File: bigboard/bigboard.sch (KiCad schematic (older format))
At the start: 38 parts, among them J1 motorA, J2 motorB, J3 USB_B_Mini, J4 device2, J5 device1, J6 battery, Q1 BSS138, Q2 BSS138, Q3 BSS138, Q4 BSS138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

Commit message: fix and design of big board
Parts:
- removed C4: 22u, symbol Device:C
- removed FB1: ferrit, symbol Device:Ferrite_Bead_Small
- removed Q1, Q2, Q3, Q4, Q5: BSS138, Package_TO_SOT_SMD:SOT-23, symbol Transistor_FET:BSS138
- removed U1: TP5400, symbol TP5400:TP5400
- removed U2: ESPCAM, symbol espcam:ESPCAM
- added Q1, Q2, Q3, Q4: BC547, Package_TO_SOT_THT:TO-92_Inline, symbol Transistor_BJT:BC547
- added Q5: IRF3205, Package_TO_SOT_THT:TO-220F-3_Horizontal_TabDown, symbol Transistor_FET:IRF3205
- added R10, R9: 1k, Resistor_THT:R_Axial_DIN0204_L3.6mm_D1.6mm_P5.08mm_Horizontal, symbol Device:R
- added R11, R12: 220, Resistor_THT:R_Axial_DIN0204_L3.6mm_D1.6mm_P5.08mm_Horizontal, symbol Device:R
- added TP1: B2, TestPoint:TestPoint_Bridge_Pitch2.54mm_Drill0.7mm, symbol Connector:TestPoint
- added TP10: VOUT, TestPoint:TestPoint_Bridge_Pitch2.54mm_Drill0.7mm, symbol Connector:TestPoint
- added TP11: GND2, TestPoint:TestPoint_Bridge_Pitch2.54mm_Drill0.7mm, symbol Connector:TestPoint
- added TP12: GND, TestPoint:TestPoint_Bridge_Pitch2.54mm_Drill0.7mm, symbol Connector:TestPoint
- added TP13: VCC, TestPoint:TestPoint_Bridge_Pitch2.54mm_Drill0.7mm, symbol Connector:TestPoint
- added TP14: BAT, TestPoint:TestPoint_Bridge_Pitch2.54mm_Drill0.7mm, symbol Connector:TestPoint
- added TP15: A01, TestPoint:TestPoint_Bridge_Pitch2.54mm_Drill0.7mm, symbol Connector:TestPoint
- added TP16: A02, TestPoint:TestPoint_Bridge_Pitch2.54mm_Drill0.7mm, symbol Connector:TestPoint
- added TP17: B01, TestPoint:TestPoint_Bridge_Pitch2.54mm_Drill0.7mm, symbol Connector:TestPoint
- added TP18: B02, TestPoint:TestPoint_Bridge_Pitch2.54mm_Drill0.7mm, symbol Connector:TestPoint
- added TP19: RXD, TestPoint:TestPoint_Bridge_Pitch2.54mm_Drill0.7mm, symbol Connector:TestPoint
- added TP2: B1, TestPoint:TestPoint_Bridge_Pitch2.54mm_Drill0.7mm, symbol Connector:TestPoint
- added TP20: TXD, TestPoint:TestPoint_Bridge_Pitch2.54mm_Drill0.7mm, symbol Connector:TestPoint
- added TP21: RTS, TestPoint:TestPoint_Bridge_Pitch2.54mm_Drill0.7mm, symbol Connector:TestPoint
- added TP22: DTR, TestPoint:TestPoint_Bridge_Pitch2.54mm_Drill0.7mm, symbol Connector:TestPoint
- added TP23: ESPen, TestPoint:TestPoint_Bridge_Pitch2.54mm_Drill0.7mm, symbol Connector:TestPoint
- added TP3: A2, TestPoint:TestPoint_Bridge_Pitch2.54mm_Drill0.7mm, symbol Connector:TestPoint
- added TP4: A1, TestPoint:TestPoint_Bridge_Pitch2.54mm_Drill0.7mm, symbol Connector:TestPoint
- added TP5: PWMa, TestPoint:TestPoint_Bridge_Pitch2.54mm_Drill0.7mm, symbol Connector:TestPoint
- added TP6: PWMb, TestPoint:TestPoint_Bridge_Pitch2.54mm_Drill0.7mm, symbol Connector:TestPoint
- added TP7: LX, TestPoint:TestPoint_Bridge_Pitch2.54mm_Drill0.7mm, symbol Connector:TestPoint
- added TP8: DEV1, TestPoint:TestPoint_Bridge_Pitch2.54mm_Drill0.7mm, symbol Connector:TestPoint
- added TP9: DEV2, TestPoint:TestPoint_Bridge_Pitch2.54mm_Drill0.7mm, symbol Connector:TestPoint
- added U1: ESPCAM, espcam:ESPCAM_bottom, symbol espcam:ESPCAM
- added U2: TP5400, TP5400:ESOP8-F.Cu-only, symbol TP5400:TP5400
- C1, C10, C5, C6, C9: footprint (none) -> Capacitor_THT:C_Disc_D3.0mm_W1.6mm_P2.50mm
- C2, C7: footprint (none) -> Capacitor_THT:CP_Radial_D10.0mm_P2.50mm_P5.00mm
- C3: value 22u -> 47u; footprint (none) -> Capacitor_THT:CP_Radial_D10.0mm_P2.50mm_P5.00mm
- C8: footprint (none) -> Capacitor_THT:C_Disc_D4.3mm_W1.9mm_P5.00mm
- D1: footprint (none) -> Diode_THT:D_A-405_P7.62mm_Horizontal
- D2, D3: footprint (none) -> LED_THT:LED_D3.0mm
- J3: footprint (none) -> Connector_USB:USB_Micro-B_Molex-105017-0001
- J6: footprint (none) -> Connector_PinHeader_2.54mm:PinHeader_1x02_P2.54mm_Vertical
- L1: footprint (none) -> Inductor_THT:L_Toroid_Vertical_L10.0mm_W5.0mm_P5.08mm
- R1, R2, R3, R4, R5, R6, R7, R8: footprint (none) -> Resistor_THT:R_Axial_DIN0204_L3.6mm_D1.6mm_P5.08mm_Horizontal
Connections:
- net labels added: A01, A02, B01, BO2, ESPen
- wire segments 180 -> 186
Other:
- note added: "testpoints\n"

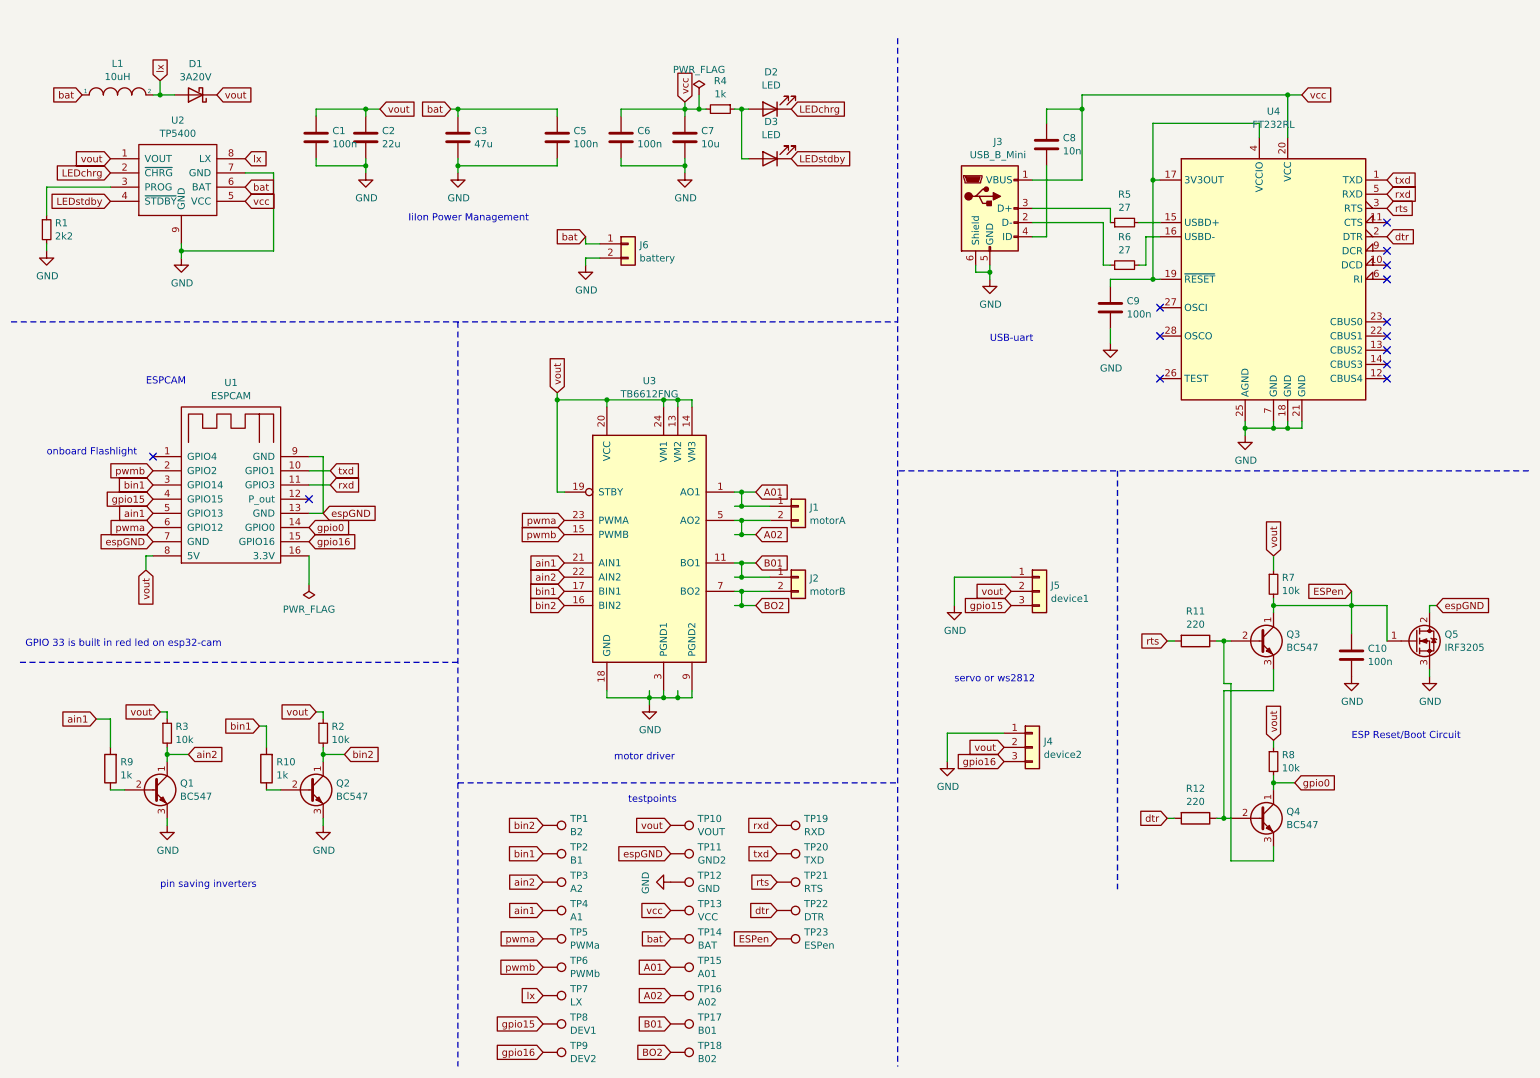
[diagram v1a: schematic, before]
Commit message: Fix Footprints for kicad 5.1.8
thanks to tobi for the tip how to install a newer
kicad on debian: there is a newer version in
debian-packports.

fixed the libraries and footprints, and changed
the path to relative ones.
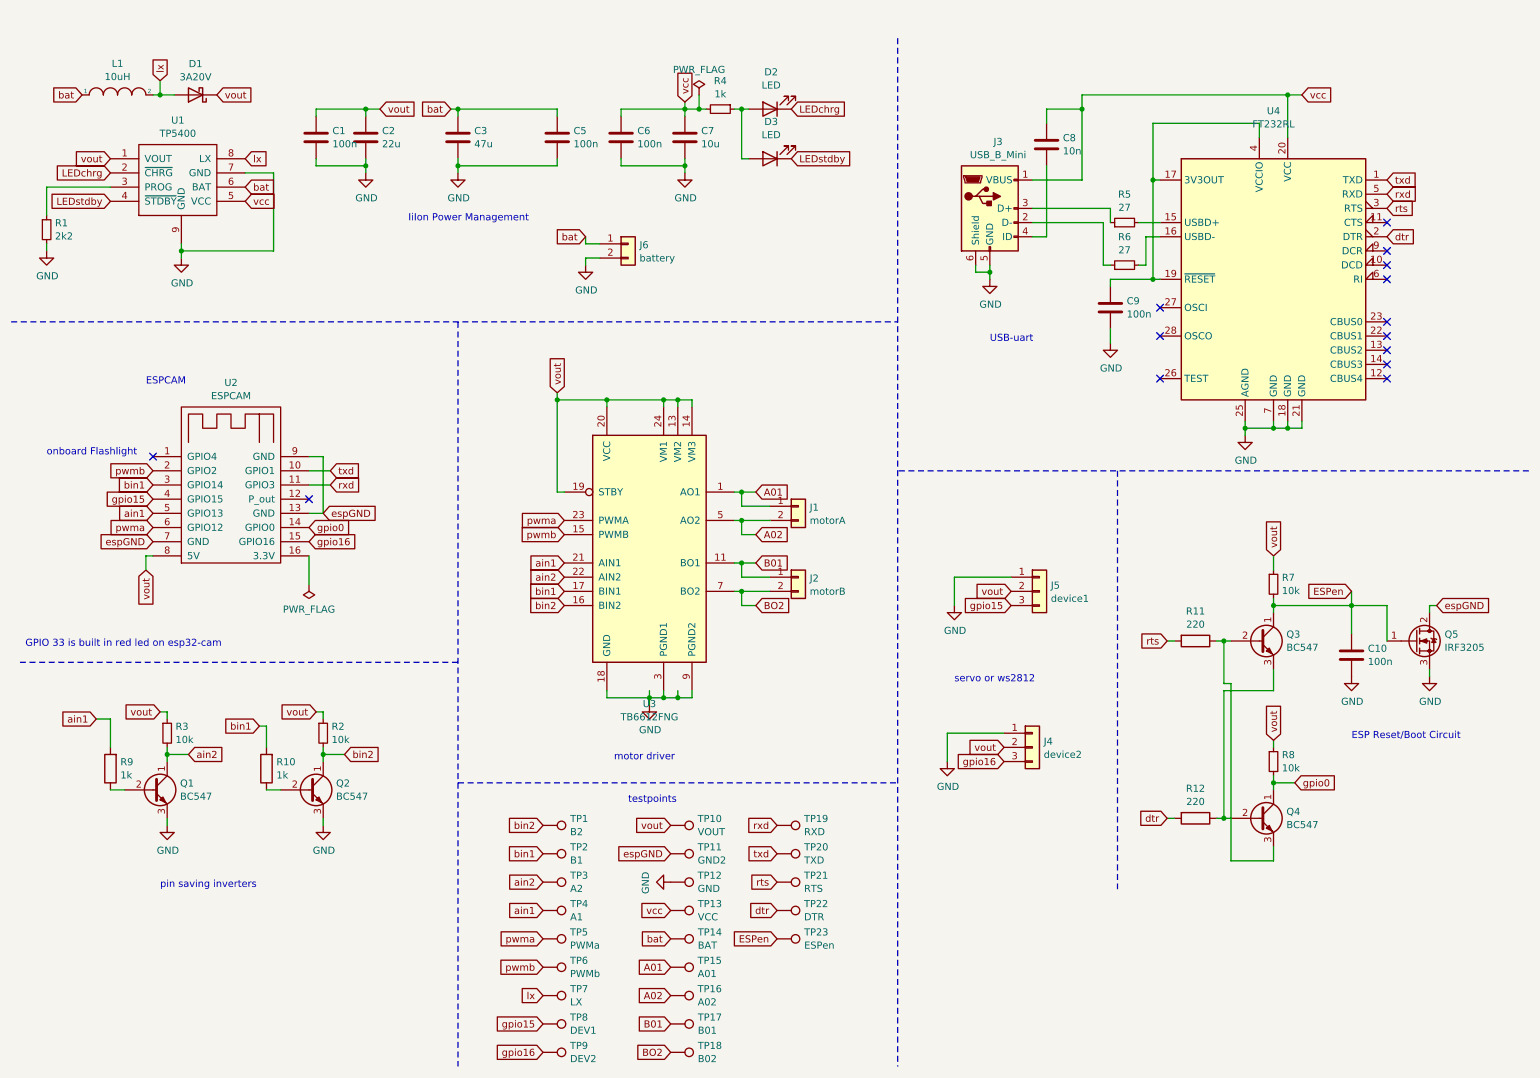
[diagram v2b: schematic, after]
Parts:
- removed U1: ESPCAM, espcam:ESPCAM_bottom, symbol espcam:ESPCAM
- removed U2: TP5400, TP5400:ESOP8-F.Cu-only, symbol TP5400:TP5400
- added U1: TP5400, TP5400:ESOP8-F.Cu-only, symbol TP5400:TP5400
- added U2: ESPCAM, espcam:ESPCAM_bottom, symbol espcam:ESPCAM
- J3: footprint Connector_USB:USB_Micro-B_Molex-105017-0001 -> Connector_USB:USB_Micro-B_Amphenol_10118194_Horizontal
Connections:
- wire segments 186 -> 182
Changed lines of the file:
@@
 EESchema Schematic File Version 4
-EELAYER 26 0
+EELAYER 30 0
 EELAYER END
 $Descr A4 11693 8268
@@
 Comment4 ""
 $EndDescr
-$Comp
-L TP5400:TP5400 U2
-U 1 1 600C44C1
-P 1700 1250
-F 0 "U2" H 1675 1421 50  0000 C CNN
-F 1 "TP5400" H 1675 1328 50  0000 C CNN
-F 2 "TP5400:ESOP8-F.Cu-only" H 1700 1250 50  0001 C CNN
-F 3 "" H 1700 1250 50  0001 C CNN
-	1    1700 1250
-	1    0    0    -1
-$EndComp
 Text GLabel 2150 1550 2    50   Input ~ 0
 bat
@@
 vcc
 $Comp
-L Connector:USB_B_Mini J3
-U 1 1 600CF507
-P 7400 1700
-F 0 "J3" H 7457 2170 50  0000 C CNN
-F 1 "USB_B_Mini" H 7457 2077 50  0000 C CNN
-F 2 "Connector_USB:USB_Micro-B_Molex-105017-0001" H 7550 1650 50  0001 C CNN
-F 3 "~" H 7550 1650 50  0001 C CNN
-	1    7400 1700
-	1    0    0    -1
-$EndComp
-$Comp
 L Device:C C8
 U 1 1 600CF5B2
@@
 Wire Wire Line
 	2750 3650 2600 3650
-$Comp
-L Interface_USB:FT232RL U4
-U 1 1 600F945A
-P 9400 2200
-F 0 "U4" H 9400 3384 50  0000 C CNN
-F 1 "FT232RL" H 9400 3291 50  0000 C CNN
-F 2 "Package_SO:SSOP-28_5.3x10.2mm_P0.65mm" H 9400 2200 50  0001 C CNN
-F 3 "http://www.ftdichip.com/Products/ICs/FT232RL.htm" H 9400 2200 50  0001 C CNN
-	1    9400 2200
-	1    0    0    -1
-$EndComp
 Wire Wire Line
 	8250 2550 8250 2650
@@
 Connection ~ 9200 3250
 $Comp
-L Driver_Motor:TB6612FNG U3
-U 1 1 6012F17F
-P 5000 4100
-F 0 "U3" H 5000 5284 50  0000 C CNN
-F 1 "TB6612FNG" H 5000 5191 50  0000 C CNN
-F 2 "Package_SO:SSOP-24_5.3x8.2mm_P0.65mm" H 5450 4700 50  0001 C CNN
-F 3 "https://toshiba.semicon-storage.com/us/product/linear/motordriver/detail.TB6612FNG.html" H 5450 4700 50  0001 C CNN
-	1    5000 4100
-	1    0    0    -1
-$EndComp
-$Comp
 L Connector_Generic:Conn_01x02 J1
 U 1 1 6012F397
@@
 	5650 3700 5650 3800
 Wire Wire Line
-	5650 3800 5600 3800
-Wire Wire Line
 	5650 3800 5850 3800
-Connection ~ 5650 3800
 Wire Wire Line
 	5600 3900 5650 3900
-Wire Wire Line
-	5600 4000 5650 4000
 Wire Wire Line
 	5650 4000 5650 3900
@@
 	5650 4200 5650 4300
 Wire Wire Line
-	5650 4300 5600 4300
-Wire Wire Line
 	5650 4300 5850 4300
-Connection ~ 5650 4300
 Wire Wire Line
 	5600 4400 5650 4400
-Wire Wire Line
-	5600 4500 5650 4500
 Wire Wire Line
 	5650 4500 5650 4400
@@
 	8050 900  9500 900
 $Comp
-L espcam:ESPCAM U1
-U 1 1 600F596E
-P 2050 3350
-F 0 "U1" H 2050 3771 50  0000 C CNN
-F 1 "ESPCAM" H 2050 3678 50  0000 C CNN
-F 2 "espcam:ESPCAM_bottom" H 2050 3350 50  0001 C CNN
-F 3 "" H 2050 3350 50  0001 C CNN
-	1    2050 3350
-	1    0    0    -1
-$EndComp
-$Comp
 L Device:R R11
 U 1 1 600F61BE
@@
 Wire Wire Line
 	5750 4000 5650 4000
-Connection ~ 5650 4000
 Wire Wire Line
 	5750 4200 5650 4200
@@
 Wire Wire Line
 	5750 4500 5650 4500
-Connection ~ 5650 4500
 Text GLabel 9950 4400 0    50   Input ~ 0
 ESPen
@@
 Wire Wire Line
 	9100 5050 9100 6300
+$Comp
+L Driver_Motor:TB6612FNG U3
+U 1 1 601168A3
+P 5000 4100
+F 0 "U3" H 5000 3007 50  0000 C CNN
+F 1 "TB6612FNG" H 5000 2914 50  0000 C CNN
+F 2 "Package_SO:SSOP-24_5.3x8.2mm_P0.65mm" H 6300 3200 50  0001 C CNN
+F 3 "https://toshiba.semicon-storage.com/us/product/linear/motordriver/detail.TB6612FNG.html" H 5450 4700 50  0001 C CNN
+	1    5000 4100
+	1    0    0    -1
+$EndComp
+$Comp
+L Interface_USB:FT232RL U4
+U 1 1 6011BB52
+P 9400 2200
+F 0 "U4" H 9400 3387 50  0000 C CNN
+F 1 "FT232RL" H 9400 3294 50  0000 C CNN
+F 2 "Package_SO:SSOP-28_5.3x10.2mm_P0.65mm" H 10500 1300 50  0001 C CNN
+F 3 "https://www.ftdichip.com/Support/Documents/DataSheets/ICs/DS_FT232R.pdf" H 9400 2200 50  0001 C CNN
+	1    9400 2200
+	1    0    0    -1
+$EndComp
+$Comp
+L Connector:USB_B_Mini J3
+U 1 1 6011DE25
+P 7400 1700
+F 0 "J3" H 7458 2170 50  0000 C CNN
+F 1 "USB_B_Mini" H 7458 2077 50  0000 C CNN
+F 2 "Connector_USB:USB_Micro-B_Amphenol_10118194_Horizontal" H 7550 1650 50  0001 C CNN
+F 3 "~" H 7550 1650 50  0001 C CNN
+	1    7400 1700
+	1    0    0    -1
+$EndComp
+$Comp
+L TP5400:TP5400 U1
+U 1 1 6011F43C
+P 1700 1250
+F 0 "U1" H 1675 1421 50  0000 C CNN
+F 1 "TP5400" H 1675 1328 50  0000 C CNN
+F 2 "TP5400:ESOP8-F.Cu-only" H 1700 1250 50  0001 C CNN
+F 3 "" H 1700 1250 50  0001 C CNN
+	1    1700 1250
+	1    0    0    -1
+$EndComp
+$Comp
+L espcam:ESPCAM U2
+U 1 1 60121F9D
+P 2050 3350
+F 0 "U2" H 2050 3771 50  0000 C CNN
+F 1 "ESPCAM" H 2050 3678 50  0000 C CNN
+F 2 "espcam:ESPCAM_bottom" H 2050 3350 50  0001 C CNN
+F 3 "" H 2050 3350 50  0001 C CNN
+	1    2050 3350
+	1    0    0    -1
+$EndComp
 $EndSCHEMATC
